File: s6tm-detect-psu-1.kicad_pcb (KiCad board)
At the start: 4 copper layers, 50 x 50 mm, 120 parts, among them J1 Conn_01x02, J2 Conn_01x02, J3 USB_C_Receptacle_USB2.0_14P, J4 Conn_01x04, J5 Conn_01x04, J6 Conn_01x04_Pin, J7 TC2030, SW1 SW_Push, SW2 SW_Push, U1 TPS259470x, U2 TPS259470x, U3 TPS259470x, U4 TPS62933, U5 TPS259470x, U6 SN65HVD230, U7 HT753-1, U8 STM32F103C8Tx, Y1 8M

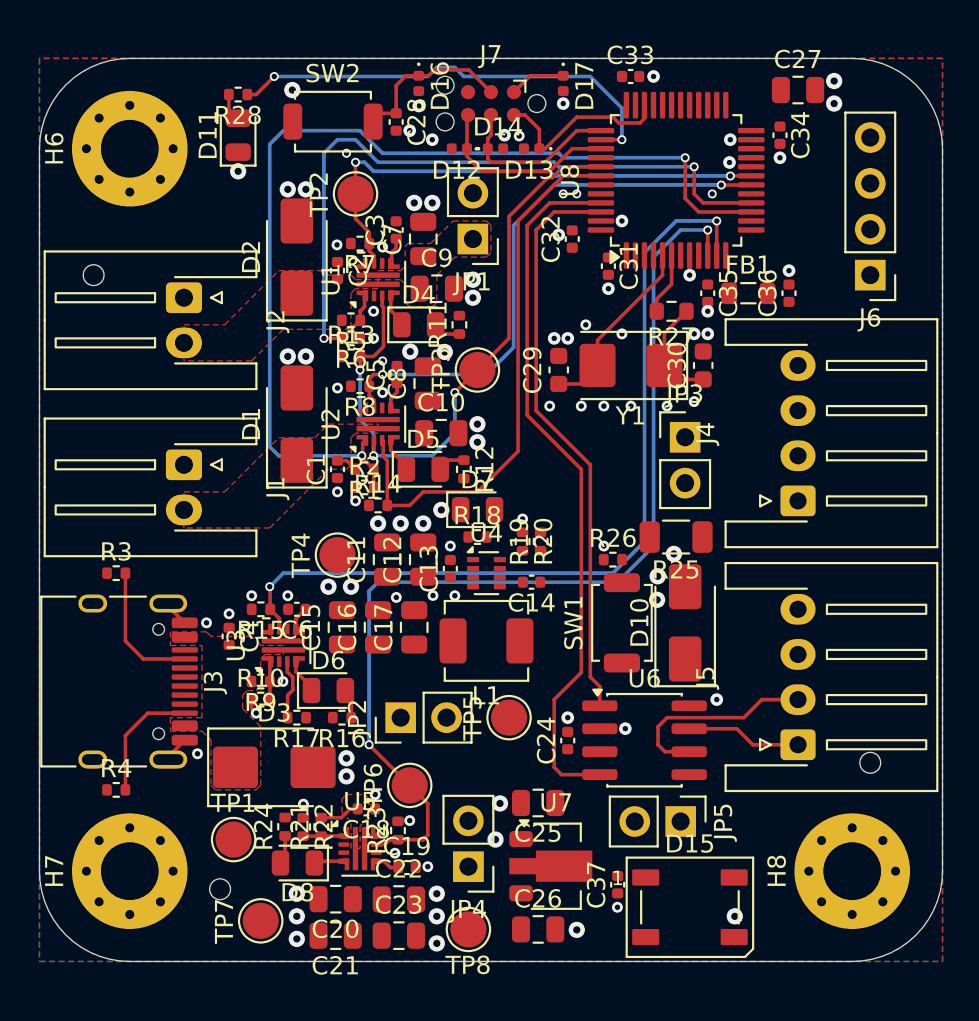
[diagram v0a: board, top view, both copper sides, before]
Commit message: pcb: route efuse gpios
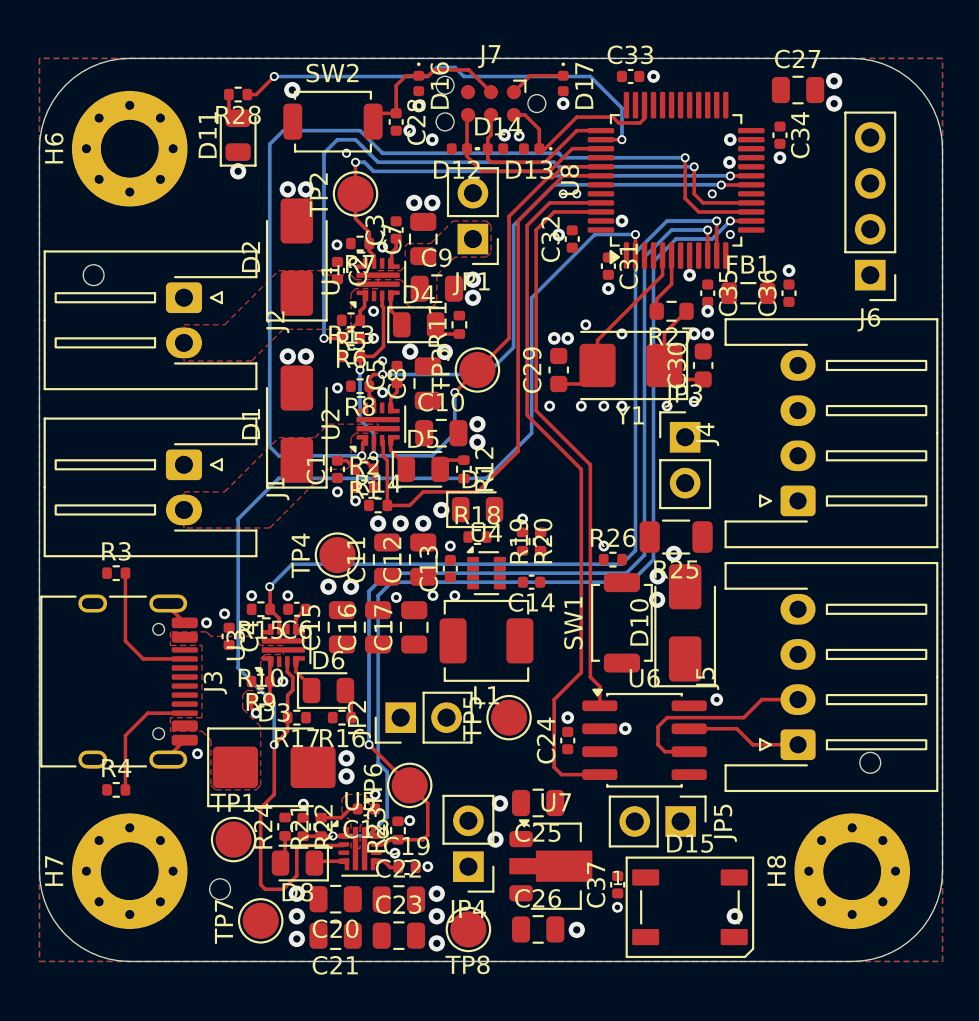
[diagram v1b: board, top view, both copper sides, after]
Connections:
- U8 pad 2: unconnected-(U8-PC13-Pad2) -> IN3
- U8 pad 32: IN3 -> unconnected-(U8-PA11-Pad32)
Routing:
- net IN3: track 3.35 -> 67.2 mm, vias 0 -> 2
- net 5_V: track 2.25 -> 57.1 mm, vias 0 -> 2
- net GND: vias 100 -> 101

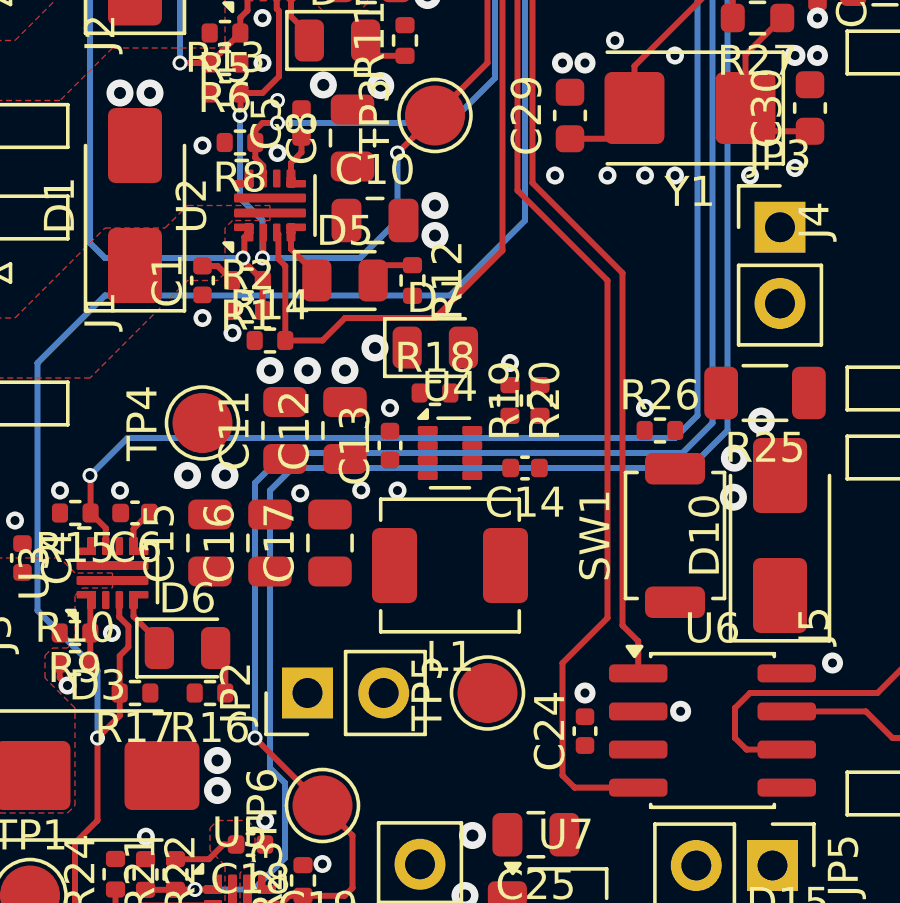
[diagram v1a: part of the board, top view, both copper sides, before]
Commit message: pcb: add smps routing
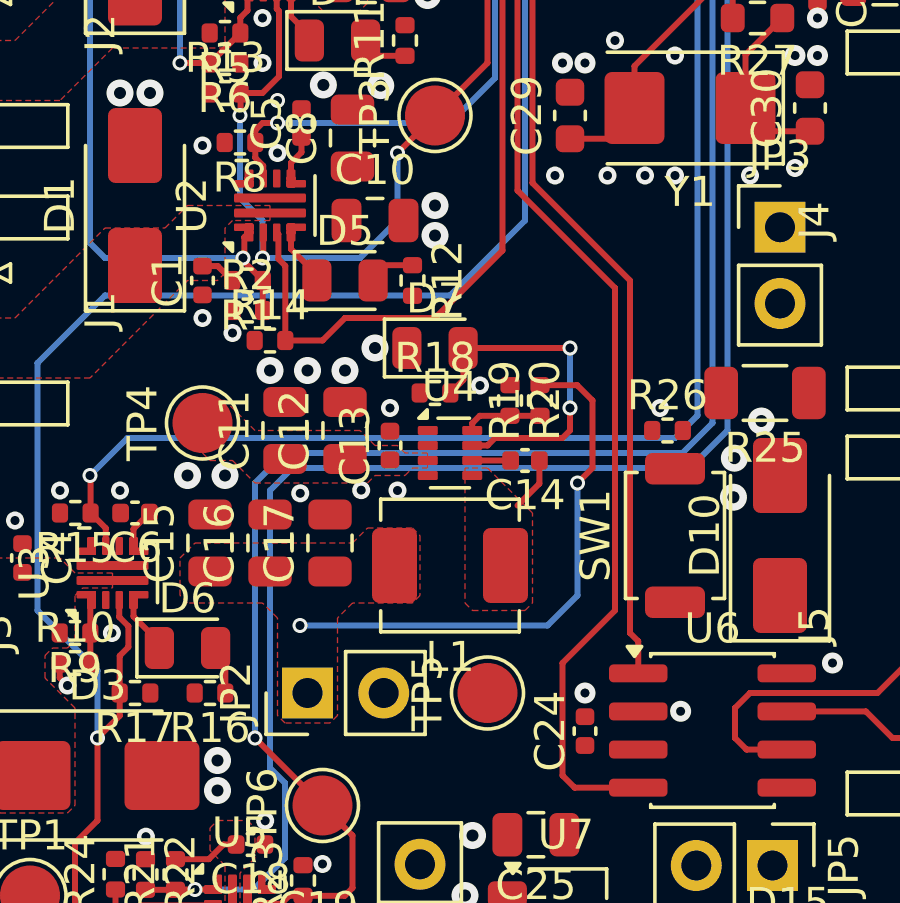
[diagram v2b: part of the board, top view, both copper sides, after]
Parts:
- moved C14 0.25 mm to (126.2, 134.8)
- moved R26 0.25 mm to (131.0, 133.8)
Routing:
- net +5V_SMPS: track 2.22 -> 20.6 mm, vias 0 -> 2
- net Net-(D7-A): track 0.00 -> 11.5 mm, vias 0 -> 2
- net Net-(U4-FB): track 0.00 -> 2.60 mm
- net Net-(U4-SW): track 0.00 -> 1.80 mm
- net Net-(U4-BST): track 0.00 -> 1.28 mm
- added copper zone on F.Cu, net Net-(U4-SW)

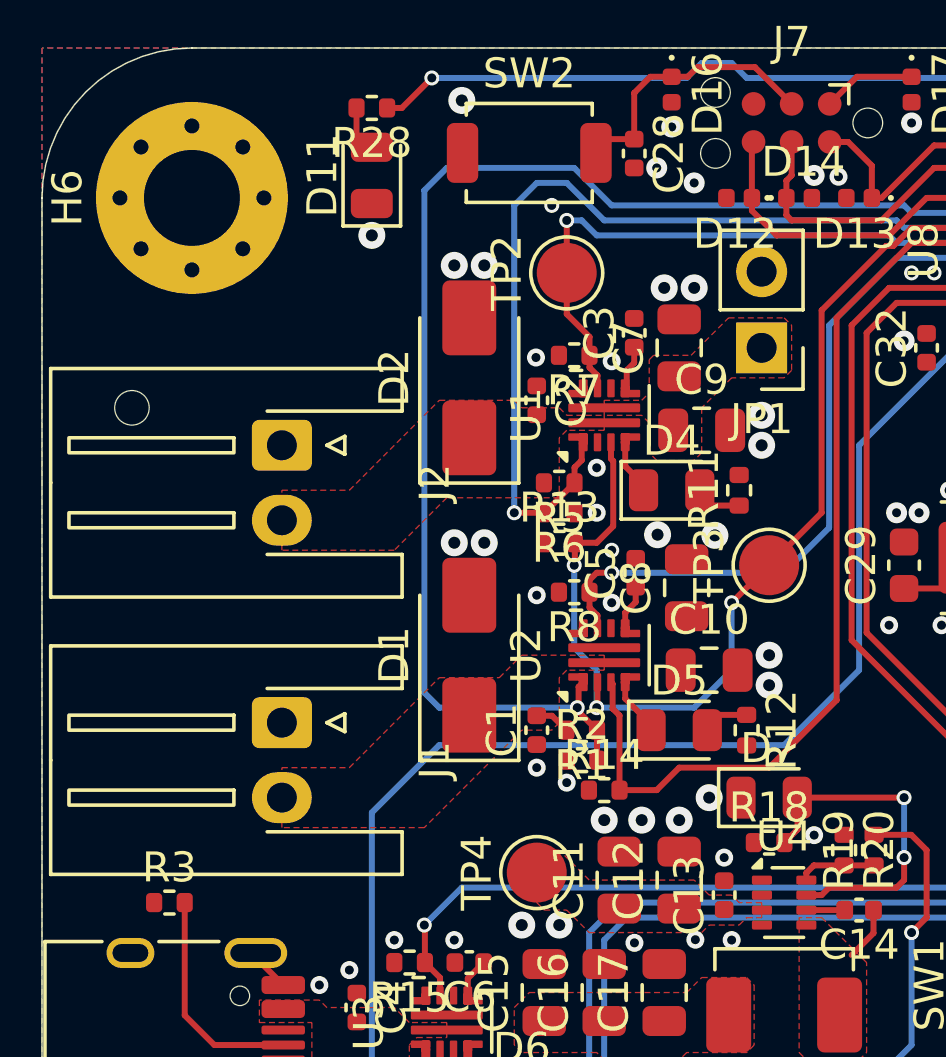
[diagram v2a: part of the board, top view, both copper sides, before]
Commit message: pcb: add +batt routing
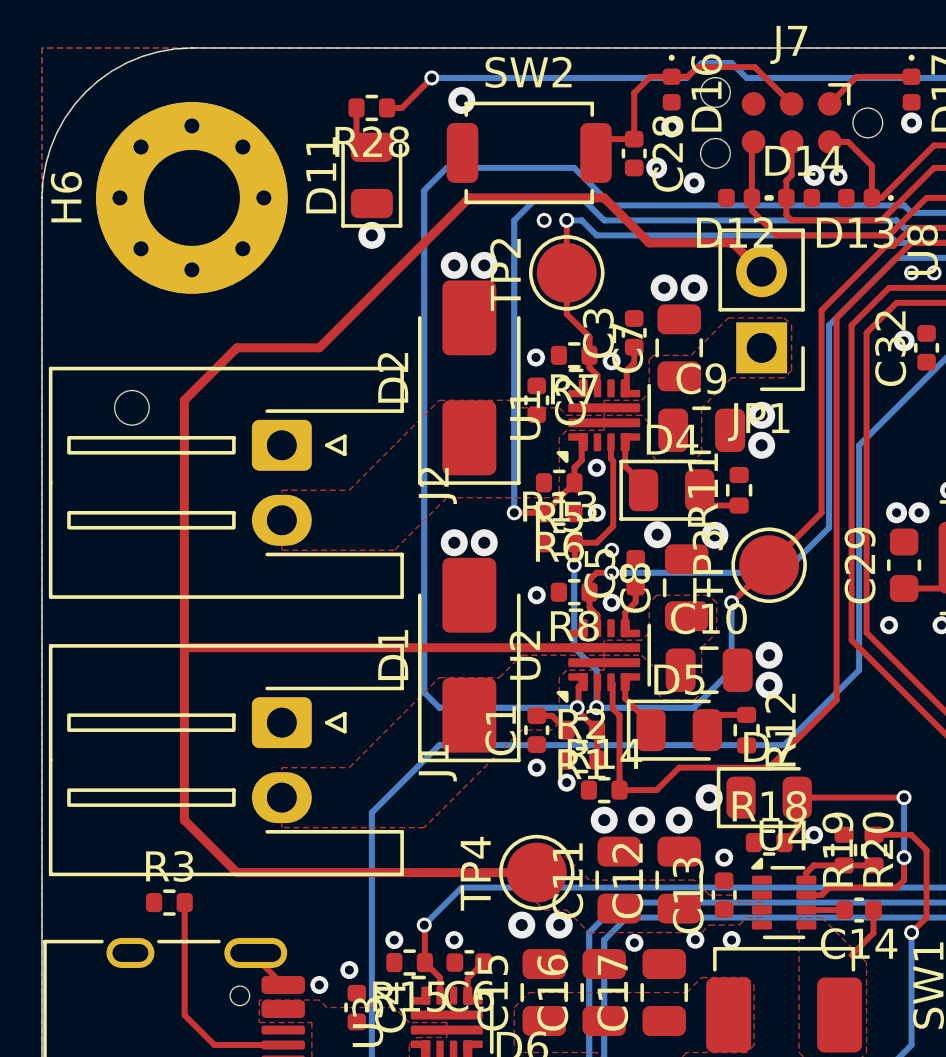
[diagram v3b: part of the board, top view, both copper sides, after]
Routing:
- net +BATT: track 0.00 -> 63.5 mm
- net BATT1_V: track 40.4 -> 39.7 mm
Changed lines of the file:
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@@
 	)
 	(via
-		(at 116 111.25)
+		(at 115.75 111.75)
 		(size 0.5)
 		(drill 0.3)
@@
 	)
 	(segment
-		(start 115.5 110.5)
-		(end 116.5 110.5)
+		(start 114.75 121.5)
+		(end 114.75 111.75)
 		(width 0.2)
 		(layer "B.Cu")
@@
 	)
 	(segment
-		(start 114.75 111.25)
-		(end 115.5 110.5)
+		(start 127.5 111.75)
+		(end 127.75 112)
+		(width 0.2)
+		(layer "B.Cu")
+		(net "BATT1_V")
+	)
+	(segment
+		(start 127.75 112)
+		(end 135.25 112)
 		(width 0.2)
 		(layer "B.Cu")
@@
 	)
 	(segment
-		(start 116.5 110.5)
+		(start 117 111)
 		(end 117.75 111.75)
 		(width 0.2)
@@
 	)
 	(segment
-		(start 127.75 112)
-		(end 135.25 112)
+		(start 114.75 111.75)
+		(end 115.5 111)
 		(width 0.2)
 		(layer "B.Cu")
@@
 	)
 	(segment
-		(start 127.5 111.75)
-		(end 127.75 112)
-		(width 0.2)
-		(layer "B.Cu")
-		(net "BATT1_V")
-	)
-	(segment
-		(start 114.75 121.5)
-		(end 114.75 111.25)
+		(start 115.5 111)
+		(end 117 111)
 		(width 0.2)
 		(layer "B.Cu")
@@
 		(layer "F.Cu")
 		(net "/Logic/CAN_TX")
+	)
+	(segment
+		(start 122.04 112.5)
+		(end 123 113.46)
+		(width 0.3)
+		(layer "F.Cu")
+		(net "+BATT")
+	)
+	(segment
+		(start 105.5 116)
+		(end 108.25 116)
+		(width 0.3)
+		(layer "F.Cu")
+		(net "+BATT")
+	)
+	(segment
+		(start 117.75 111)
+		(end 119.25 112.5)
+		(width 0.3)
+		(layer "F.Cu")
+		(net "+BATT")
+	)
+	(segment
+		(start 119.25 112.5)
+		(end 122.04 112.5)
+		(width 0.3)
+		(layer "F.Cu")
+		(net "+BATT")
+	)
+	(segment
+		(start 105.5 133.5)
+		(end 103.75 131.75)
+		(width 0.3)
+		(layer "F.Cu")
+		(net "+BATT")
+	)
+	(segment
+		(start 103.75 126)
+		(end 103.75 117.75)
+		(width 0.3)
+		(layer "F.Cu")
+		(net "+BATT")
+	)
+	(segment
+		(start 115.5 133.5)
+		(end 105.5 133.5)
+		(width 0.3)
+		(layer "F.Cu")
+		(net "+BATT")
+	)
+	(segment
+		(start 117.75 126)
+		(end 103.75 126)
+		(width 0.3)
+		(layer "F.Cu")
+		(net "+BATT")
+	)
+	(segment
+		(start 108.25 116)
+		(end 113.25 111)
+		(width 0.3)
+		(layer "F.Cu")
+		(net "+BATT")
+	)
+	(segment
+		(start 103.75 117.75)
+		(end 105.5 116)
+		(width 0.3)
+		(layer "F.Cu")
+		(net "+BATT")
+	)
+	(segment
+		(start 113.25 111)
+		(end 117.75 111)
+		(width 0.3)
+		(layer "F.Cu")
+		(net "+BATT")
+	)
+	(segment
+		(start 103.75 131.75)
+		(end 103.75 126)
+		(width 0.3)
+		(layer "F.Cu")
+		(net "+BATT")
 	)
 	(segment
@@
 			)
 		)
+	)
+	(zone
+		(net "+BATT")
+		(layer "F.Cu")
+		(hatch edge 0.5)
+		(priority 9)
+		(connect_pads yes
+			(clearance 0.2)
+		)
+		(min_thickness 0.15)
+		(fill yes
+			(thermal_gap 0.5)
+			(thermal_bridge_width 0.5)
+			(island_removal_mode 0)
+		)
+		(polygon
+			(pts
+				(xy 117.75 126.25) (xy 119 126.25) (xy 119.5 126.75) (xy 119.5 127.5) (xy 119.75 127.75) (xy 120.75 127.75)
+				(xy 121 127.5) (xy 121 126) (xy 121.5 125.5) (xy 121.5 124.5) (xy 121.25 124.25) (xy 119.5 124.25)
+				(xy 119.25 124.5) (xy 119.25 125.5) (xy 119 125.75) (xy 117.75 125.75)
+			)
+		)

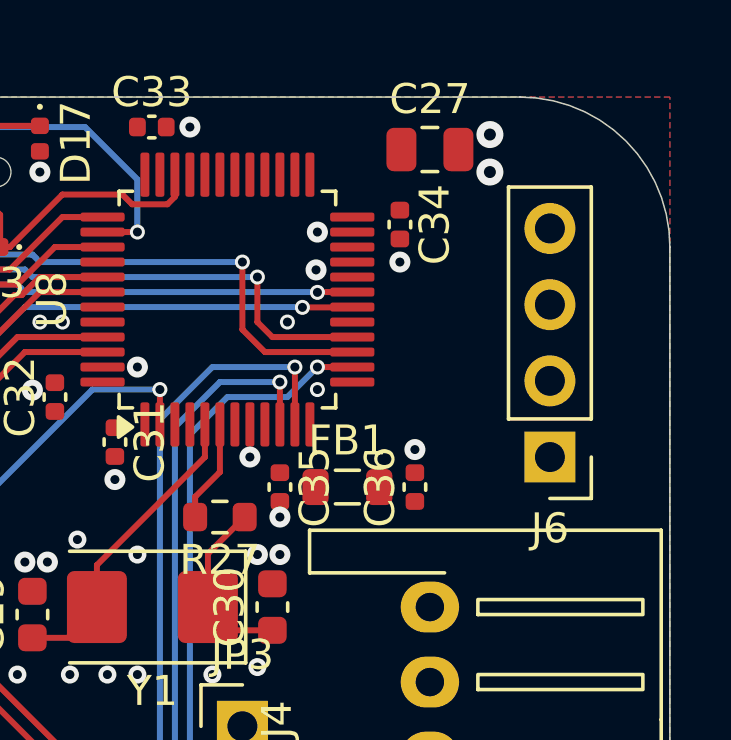
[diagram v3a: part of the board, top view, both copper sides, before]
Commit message: pcb: add uart routing
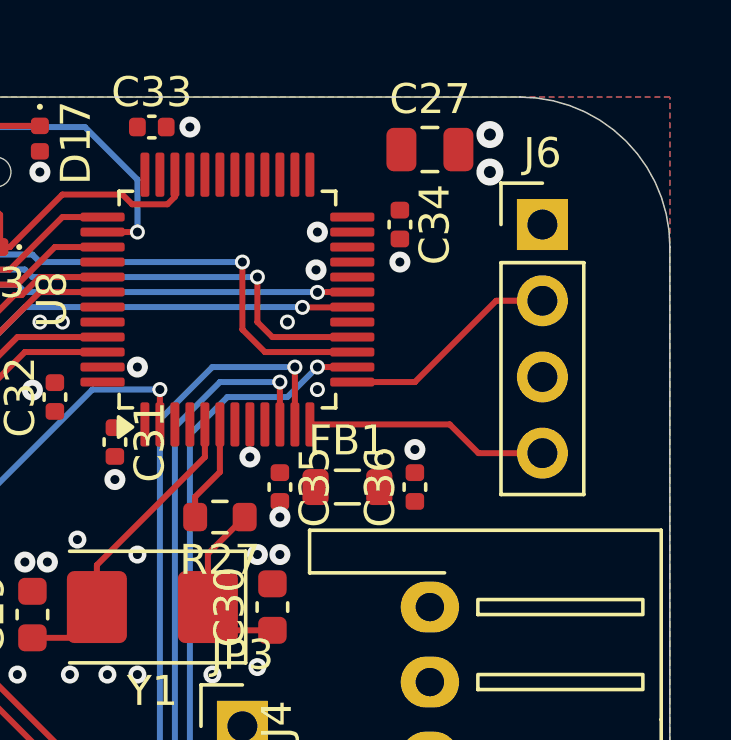
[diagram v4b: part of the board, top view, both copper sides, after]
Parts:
- moved J6 7.75 mm to (144.8, 110.2), turned to 0 degrees
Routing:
- net /Logic/U0TXD: track 0.00 -> 8.15 mm
- net /Logic/U0RXD: track 0.00 -> 7.46 mm
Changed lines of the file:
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@@
 	(footprint "Connector_PinHeader_2.54mm:PinHeader_1x04_P2.54mm_Vertical"
 		(layer "F.Cu")
-		(at 145 118 180)
+		(at 144.75 110.25)
 		(descr "Through hole straight pin header, 1x04, 2.54mm pitch, single row")
 		(tags "Through hole pin header THT 1x04 2.54mm single row")
@@
 		(duplicate_pad_numbers_are_jumpers no)
 		(fp_line
-			(start 1.38 1.27)
-			(end 1.38 9)
+			(start -1.38 -1.38)
+			(end 0 -1.38)
 			(stroke
 				(width 0.12)
@@
 		)
 		(fp_line
-			(start -1.38 9)
-			(end 1.38 9)
+			(start -1.38 0)
+			(end -1.38 -1.38)
 			(stroke
 				(width 0.12)
@@
 		(fp_line
 			(start -1.38 1.27)
-			(end 1.38 1.27)
+			(end -1.38 9)
 			(stroke
 				(width 0.12)
@@
 		(fp_line
 			(start -1.38 1.27)
-			(end -1.38 9)
+			(end 1.38 1.27)
 			(stroke
 				(width 0.12)
@@
 		)
 		(fp_line
-			(start -1.38 0)
-			(end -1.38 -1.38)
+			(start -1.38 9)
+			(end 1.38 9)
 			(stroke
 				(width 0.12)
@@
 		)
 		(fp_line
-			(start -1.38 -1.38)
-			(end 0 -1.38)
+			(start 1.38 1.27)
+			(end 1.38 9)
 			(stroke
 				(width 0.12)
@@
 		)
 		(fp_line
-			(start 1.27 8.89)
-			(end -1.27 8.89)
+			(start -1.27 -0.635)
+			(end -0.635 -1.27)
 			(stroke
 				(width 0.1)
@@
 		)
 		(fp_line
-			(start 1.27 -1.27)
-			(end 1.27 8.89)
+			(start -1.27 8.89)
+			(end -1.27 -0.635)
 			(stroke
 				(width 0.1)
@@
 		)
 		(fp_line
-			(start -1.27 8.89)
-			(end -1.27 -0.635)
+			(start 1.27 -1.27)
+			(end 1.27 8.89)
 			(stroke
 				(width 0.1)
@@
 		)
 		(fp_line
-			(start -1.27 -0.635)
-			(end -0.635 -1.27)
+			(start 1.27 8.89)
+			(end -1.27 8.89)
 			(stroke
 				(width 0.1)
@@
 		)
 		(pad "1" thru_hole rect
-			(at 0 0 180)
+			(at 0 0)
 			(size 1.7 1.7)
 			(drill 1)
@@
 		)
 		(pad "2" thru_hole circle
-			(at 0 2.54 180)
+			(at 0 2.54)
 			(size 1.7 1.7)
 			(drill 1)
@@
 		)
 		(pad "3" thru_hole circle
-			(at 0 5.08 180)
+			(at 0 5.08)
 			(size 1.7 1.7)
 			(drill 1)
@@
 		)
 		(pad "4" thru_hole circle
-			(at 0 7.62 180)
+			(at 0 7.62)
 			(size 1.7 1.7)
 			(drill 1)
@@
 	)
 	(segment
+		(start 142.62 117.87)
+		(end 141.6625 116.9125)
+		(width 0.2)
+		(layer "F.Cu")
+		(net "/Logic/U0TXD")
+	)
+	(segment
+		(start 144.75 117.87)
+		(end 142.62 117.87)
+		(width 0.2)
+		(layer "F.Cu")
+		(net "/Logic/U0TXD")
+	)
+	(segment
+		(start 141.6625 116.9125)
+		(end 137 116.9125)
+		(width 0.2)
+		(layer "F.Cu")
+		(net "/Logic/U0TXD")
+	)
+	(segment
+		(start 143.21 112.79)
+		(end 144.75 112.79)
+		(width 0.2)
+		(layer "F.Cu")
+		(net "/Logic/U0RXD")
+	)
+	(segment
+		(start 140.5 115.5)
+		(end 143.21 112.79)
+		(width 0.2)
+		(layer "F.Cu")
+		(net "/Logic/U0RXD")
+	)
+	(segment
+		(start 138.4125 115.5)
+		(end 140.5 115.5)
+		(width 0.2)
+		(layer "F.Cu")
+		(net "/Logic/U0RXD")
+	)
+	(segment
